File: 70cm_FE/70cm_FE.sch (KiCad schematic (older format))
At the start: 67 parts, among them J1 Conn_01x02, J2 U.FL, J3 U.FL, J4 Conn_01x02, J5 U.FL, Q1 BFU520W, U1 HT7533-1, U2 M68710L, U3 74HC14

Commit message: Add some component values, add SAW footprint, change LNA transistor
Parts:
- added C18: 2p2, Capacitor_SMD:C_0603_1608Metric, symbol Device:C
- added FL1, FL2: AFS434S3, 70cm_FE:AFS434S3, symbol 70cm_FE:AFS434S3
- added R1, R2: 100k, Resistor_SMD:R_0603_1608Metric, symbol Device:R
- C11: value C -> 10p
- C13, C16: value C -> 5p6
- L2: value L -> 15n; footprint Inductor_SMD:L_0603_1608Metric -> Inductor_SMD:L_0402_1005Metric; LCSC (none) -> C27143
- L4: value L -> 15n
- L5: value L -> 68n
- Q1: value BFU520W -> 2SC3356; footprint Package_TO_SOT_SMD:SOT-323_SC-70 -> Package_TO_SOT_SMD:SOT-23; LCSC C111541 -> C9659
- R10: renamed from R8; value 1k -> 2k2
- R24: renamed from R22; value R -> 100k
- R8: renamed from R7; value 2k2 -> 4k7
- U2: footprint 70cm_pa:M68710L -> 70cm_FE:M68710L
- renumbered C18 to C19, C19 to C20, C20 to C21, C21 to C22, J2 to J1, J3 to J2, J1 to J3, R9 to R11, R10 to R12, R11 to R13, R12 to R14, R13 to R15, R14 to R16, R15 to R17, R16 to R18, R17 to R19, R18 to R20, R19 to R21, R20 to R22, R21 to R23, R1 to R3, R2 to R4, R3 to R5, R4 to R6, R5 to R7, R6 to R9
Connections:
- wire segments 92 -> 100
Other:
- note added: "Here could be some filtering,\nalso for harmonics of the TX drive"
- note added: "TODO: driver stage"
- note added: "TODO:\njumpers to bypass SAW filters"
- note added: "TODO:\njumpers to bypass the LNA"
- note removed: "Here could be some filtering,\nat least for harmonics of the TX drive"
- note removed: "Should there be a place\nfor SAW filter here?"
- moved on the sheet: C11, C13, C16, C19, C20, C21, C22, C3, C4, C8, D2, D3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

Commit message: Add driver stage and jumpers, clean up schematic
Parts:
- removed R12, R13: 0, Resistor_SMD:R_0603_1608Metric, symbol Device:R
- added C10: 10p, Capacitor_SMD:C_0402_1005Metric, symbol Device:C
- added C11, C15, C17, C4, C5: 1n, Capacitor_SMD:C_0402_1005Metric, symbol Device:C
- added C13: 10p, Capacitor_SMD:C_0603_1608Metric, symbol Device:C
- added C14, C18: ?, Capacitor_SMD:C_0402_1005Metric, symbol Device:C
- added C32, C33, C34: DNP, Capacitor_SMD:C_0402_1005Metric, symbol Device:C
- added C6: 100p, Capacitor_SMD:C_0603_1608Metric, symbol Device:C
- added D5, D6, D7: BAV99, Package_TO_SOT_SMD:SOT-23, symbol Diode:BAV99
- added JP1, JP2, JP3, JP4, JP5, JP6: ~, 70cm_FE:Jumper-3_0402, symbol 70cm_FE:Jumper_3_Bridged12
- added L1, L6: 68n, Inductor_SMD:L_0603_1608Metric, symbol Device:L
- added L2, L5: 15n?, Inductor_SMD:L_0402_1005Metric, symbol Device:L
- added Q1, Q3: 2SC3356, Package_TO_SOT_SMD:SOT-23, symbol Device:Q_NPN_BEC
- added R1, R3: 100k, Resistor_SMD:R_0402_1005Metric, symbol Device:R
- added R10, R9: 1k, Resistor_SMD:R_0603_1608Metric, symbol Device:R
- added R14, R42: 100, Resistor_SMD:R_0603_1608Metric, symbol Device:R
- added R17, R6: 1, Resistor_SMD:R_0603_1608Metric, symbol Device:R
- added R18: 10, Resistor_SMD:R_0603_1608Metric, symbol Device:R
- added R22, R23, R25, R26, R27: 0, Resistor_SMD:R_0402_1005Metric, symbol Device:R
- added R30, R31, R32, R33, R34, R35: DNP, Resistor_SMD:R_0402_1005Metric, symbol Device:R
- added R7: 4k7, Resistor_SMD:R_0603_1608Metric, symbol Device:R
- C12: renamed from C9; footprint Capacitor_SMD:C_0603_1608Metric -> Capacitor_SMD:C_0402_1005Metric; LCSC (none) -> C1525
- C21: renamed from C10; footprint Capacitor_SMD:C_0603_1608Metric -> Capacitor_SMD:C_0402_1005Metric; LCSC (none) -> C1525
- C7: renamed from C4; value 100n -> 1n; footprint Capacitor_SMD:C_0603_1608Metric -> Capacitor_SMD:C_0402_1005Metric; LCSC (none) -> C1523
- J1: renamed from J3; value Conn_01x02 -> ~
- J5: renamed from J4; value Conn_01x02 -> ~; footprint Connector_PinHeader_2.54mm:PinHeader_1x02_P2.54mm_Vertical -> Connector_PinHeader_2.54mm:PinHeader_1x04_P2.54mm_Vertical; symbol Connector_Generic:Conn_01x02 -> Connector_Generic:Conn_01x04
- L10: renamed from L6; footprint Inductor_SMD:L_0603_1608Metric -> 70cm_FE:NetTie-2_SMD_Pad0.2mm
- L7: renamed from L4; footprint Inductor_SMD:L_0603_1608Metric -> 70cm_FE:NetTie-2_SMD_Pad0.2mm
- L9: renamed from L5; LCSC (none) -> C13415
- R2: renamed from R1; footprint Resistor_SMD:R_0603_1608Metric -> Resistor_SMD:R_0402_1005Metric
- R20: renamed from R24; footprint Resistor_SMD:R_0603_1608Metric -> Resistor_SMD:R_0402_1005Metric
- R21: renamed from R11; footprint Resistor_SMD:R_0603_1608Metric -> Resistor_SMD:R_0402_1005Metric
- R24: renamed from R17; footprint Resistor_SMD:R_0603_1608Metric -> Resistor_SMD:R_0402_1005Metric
- R28: renamed from R19; value 1k -> 100
- R29: renamed from R18; value 0 -> 100k
- R4: renamed from R2; footprint Resistor_SMD:R_0603_1608Metric -> Resistor_SMD:R_0402_1005Metric
- renumbered C8 to C16, C7 to C19, C11 to C20, C13 to C22, C16 to C23, C12 to C24, C19 to C25, C14 to C26, C15 to C27, C20 to C28, C18 to C29, C5 to C3, C21 to C30, C22 to C31, C17 to C35, C3 to C8, C6 to C9, FL2 to FL1, FL1 to FL2, J1 to J2, J2 to J3, J5 to J4, L7 to L11, L1 to L3, L2 to L4, L3 to L8, Q1 to Q2, R7 to R11, R4 to R12, R5 to R13, R8 to R15, R10 to R16, R9 to R19, R14 to R36, R20 to R37, R21 to R38, R22 to R39, R23 to R40, R16 to R41, R15 to R43, R3 to R5, R6 to R8, U3 to U2, U2 to U3
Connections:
- net labels added: DRV_EN, DRV_IN, DRV_OUT, DRV_bias, DRV_bypass, LNA_OUT, PA_EN, PIN_bias, RXSAW_IN, RXSAW_OUT, RXSAW_bypass, TXSAW_bypass, TXSAW_in, TXSAW_out, TX_ON, TX_ON_IN, TX_detect, ~TX_ON~
- net labels removed: PIN_EN, TX_EN, TX_EN_IN, ~TX_EN~
- wire segments 100 -> 176
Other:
- note added: "Control logic.\nDiodes can be used for sequencing delays."
- note added: "For better power handling, some coils are replaced\nwith long, thin microstrip lines.\nWorst-case power loss in 15 nH 0402 coil with Q=20\nfrom JLC basic series could have been around 0.5 W.\n"
- note added: "TODO: LNA bypass jumpers.\nShould the bypass branch include\nprotection diodes or not?"
- note removed: "TODO: driver stage"
- note removed: "TODO:\njumpers to bypass SAW filters"
- note removed: "TODO:\njumpers to bypass the LNA"
- moved on the sheet: C1, C12, C16, C19, C2, C20, C21, C22, C23, C24, C25, C26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

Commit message: Add RF detector, more layout
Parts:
- added C1: 1p, Capacitor_SMD:C_0402_1005Metric, symbol Device:C
- added C33: 10p, Capacitor_SMD:C_0402_1005Metric, symbol Device:C
- added D5: BAT54C, Package_TO_SOT_SMD:SOT-23, symbol Diode:BAT54C
- added R11: DNP, Resistor_SMD:R_0402_1005Metric, symbol Device:R
- added R21, R23: 100k, Resistor_SMD:R_0402_1005Metric, symbol Device:R
- added R22: 220k, Resistor_SMD:R_0402_1005Metric, symbol Device:R
- added R24, R26, R27: 1k, Resistor_SMD:R_0402_1005Metric, symbol Device:R
- added U4: LM393, Package_SO:SOIC-8_3.9x4.9mm_P1.27mm, symbol Comparator:LM393
- R10, R7, R8, R9: footprint Resistor_SMD:R_0603_1608Metric -> Resistor_SMD:R_0402_1005Metric
- R12: renamed from R13; footprint Resistor_SMD:R_0603_1608Metric -> Resistor_SMD:R_0402_1005Metric
- R14: renamed from R12; footprint Resistor_SMD:R_0603_1608Metric -> Resistor_SMD:R_0402_1005Metric
- R15: renamed from R14; footprint Resistor_SMD:R_0603_1608Metric -> Resistor_SMD:R_0402_1005Metric
- R16: renamed from R15; footprint Resistor_SMD:R_0603_1608Metric -> Resistor_SMD:R_0402_1005Metric
- R17: renamed from R16; footprint Resistor_SMD:R_0603_1608Metric -> Resistor_SMD:R_0402_1005Metric
- R19: renamed from R18; footprint Resistor_SMD:R_0603_1608Metric -> Resistor_SMD:R_0402_1005Metric
- R32: renamed from R29; footprint Resistor_SMD:R_0603_1608Metric -> Resistor_SMD:R_0402_1005Metric
- R36: renamed from R28; footprint Resistor_SMD:R_0603_1608Metric -> Resistor_SMD:R_0402_1005Metric
- R44: renamed from R37; footprint Resistor_SMD:R_0603_1608Metric -> Resistor_SMD:R_0402_1005Metric
- R45: renamed from R38; footprint Resistor_SMD:R_0603_1608Metric -> Resistor_SMD:R_0402_1005Metric
- R46: renamed from R39; footprint Resistor_SMD:R_0603_1608Metric -> Resistor_SMD:R_0402_1005Metric
- R47: renamed from R40; footprint Resistor_SMD:R_0603_1608Metric -> Resistor_SMD:R_0402_1005Metric
- R48: renamed from R41; footprint Resistor_SMD:R_0603_1608Metric -> Resistor_SMD:R_0402_1005Metric
- R49: renamed from R42; footprint Resistor_SMD:R_0603_1608Metric -> Resistor_SMD:R_0402_1005Metric
- renumbered C9 to C11, C11 to C12, C12 to C14, C14 to C15, C15 to C16, C16 to C17, C17 to C18, C18 to C19, C1 to C2, C19 to C20, C20 to C21, C21 to C22, C22 to C23, C23 to C24, C24 to C25, C25 to C26, C26 to C27, C27 to C28, C28 to C29, C2 to C3, C29 to C30, C30 to C31, C31 to C32, C32 to C34, C33 to C35, C34 to C36, C35 to C37, C3 to C4, C4 to C5, C5 to C6, C6 to C7, C7 to C8, C8 to C9, D5 to D6, D6 to D7, D7 to D8, R11 to R13, R17 to R18, R19 to R20, R20 to R25, R21 to R28, R22 to R29, R23 to R30, R24 to R31, R25 to R33, R26 to R34, R27 to R35, R30 to R37, R31 to R38, R32 to R39, R33 to R40, R34 to R41, R35 to R42, R36 to R43, R43 to R50
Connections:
- net labels added: DET_IN+, DET_IN-, DET_REF, DET_RF, DET_timing, DRV_B, DRV_C, DRV_E, LNA_B, LNA_C, LNA_E, LNA_VCC, PIN_COMRF, PIN_RXRF, PIN_TXRF, ~LNA_EN_IN~, ~LNA_EN_SEQ~, ~PA_EN_IN~, ~PA_EN_SEQ~, ~PIN_EN_IN~, ~PIN_EN_SEQ~
- wire segments 176 -> 201
- no-connect marks 0 -> 1
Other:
- note added: "TODO:\nshould the spare comparator be used\nfor overtemperature protection?"
- note removed: "TODO: RF detection"
- moved on the sheet: C11, C14, C34, C35, C36, C37, D6, D7, D8, R12, R13, R14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

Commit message: Fix control signal polarities, draft more layout
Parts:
- removed J5: ~, Connector_PinHeader_2.54mm:PinHeader_1x04_P2.54mm_Vertical, symbol Connector_Generic:Conn_01x04
- added C20: 100n, Capacitor_SMD:C_0402_1005Metric, symbol Device:C
- added R32, R44: 100, Resistor_SMD:R_0402_1005Metric, symbol Device:R
- J1: footprint Connector_PinHeader_2.54mm:PinHeader_1x02_P2.54mm_Vertical -> Connector_PinHeader_2.54mm:PinHeader_1x06_P2.54mm_Horizontal; symbol Connector_Generic:Conn_01x02 -> Connector_Generic:Conn_01x06
- R28: renamed from R32; value 100k -> 220k
- R34: renamed from R33; value 0 -> 220k
- R35: renamed from R34; value 0 -> 100k
- R39: renamed from R38; value DNP -> 0; DNP DNP -> (none)
- renumbered C12 to C11, C11 to C12, C20 to C21, C21 to C22, C22 to C23, C23 to C24, C24 to C25, C25 to C26, C26 to C27, C27 to C28, C28 to C29, C29 to C30, C30 to C31, C31 to C32, C32 to C33, C33 to C34, C34 to C35, C35 to C36, C36 to C37, C37 to C38, C5 to C4, C4 to C5, R8 to R10, R12 to R11, R11 to R12, R14 to R13, R13 to R14, R28 to R29, R29 to R30, R30 to R31, R31 to R33, R35 to R36, R36 to R37, R37 to R38, R39 to R40, R40 to R41, R41 to R42, R42 to R43, R43 to R45, R44 to R46, R45 to R47, R46 to R48, R47 to R49, R48 to R50, R49 to R51, R50 to R52, R9 to R8, R10 to R9, U4 to U3, U3 to U4
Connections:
- net labels added: DET_COMP+, DET_COMP-, DET_COMPout, DET_OUT, DET_OUT_
- net labels removed: DET_IN+, DET_IN-, TX_detect
- wire segments 201 -> 202
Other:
- moved on the sheet: C12, C14, C2, C3, C34, C5, D1, R10, R12, R14, R28, R5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

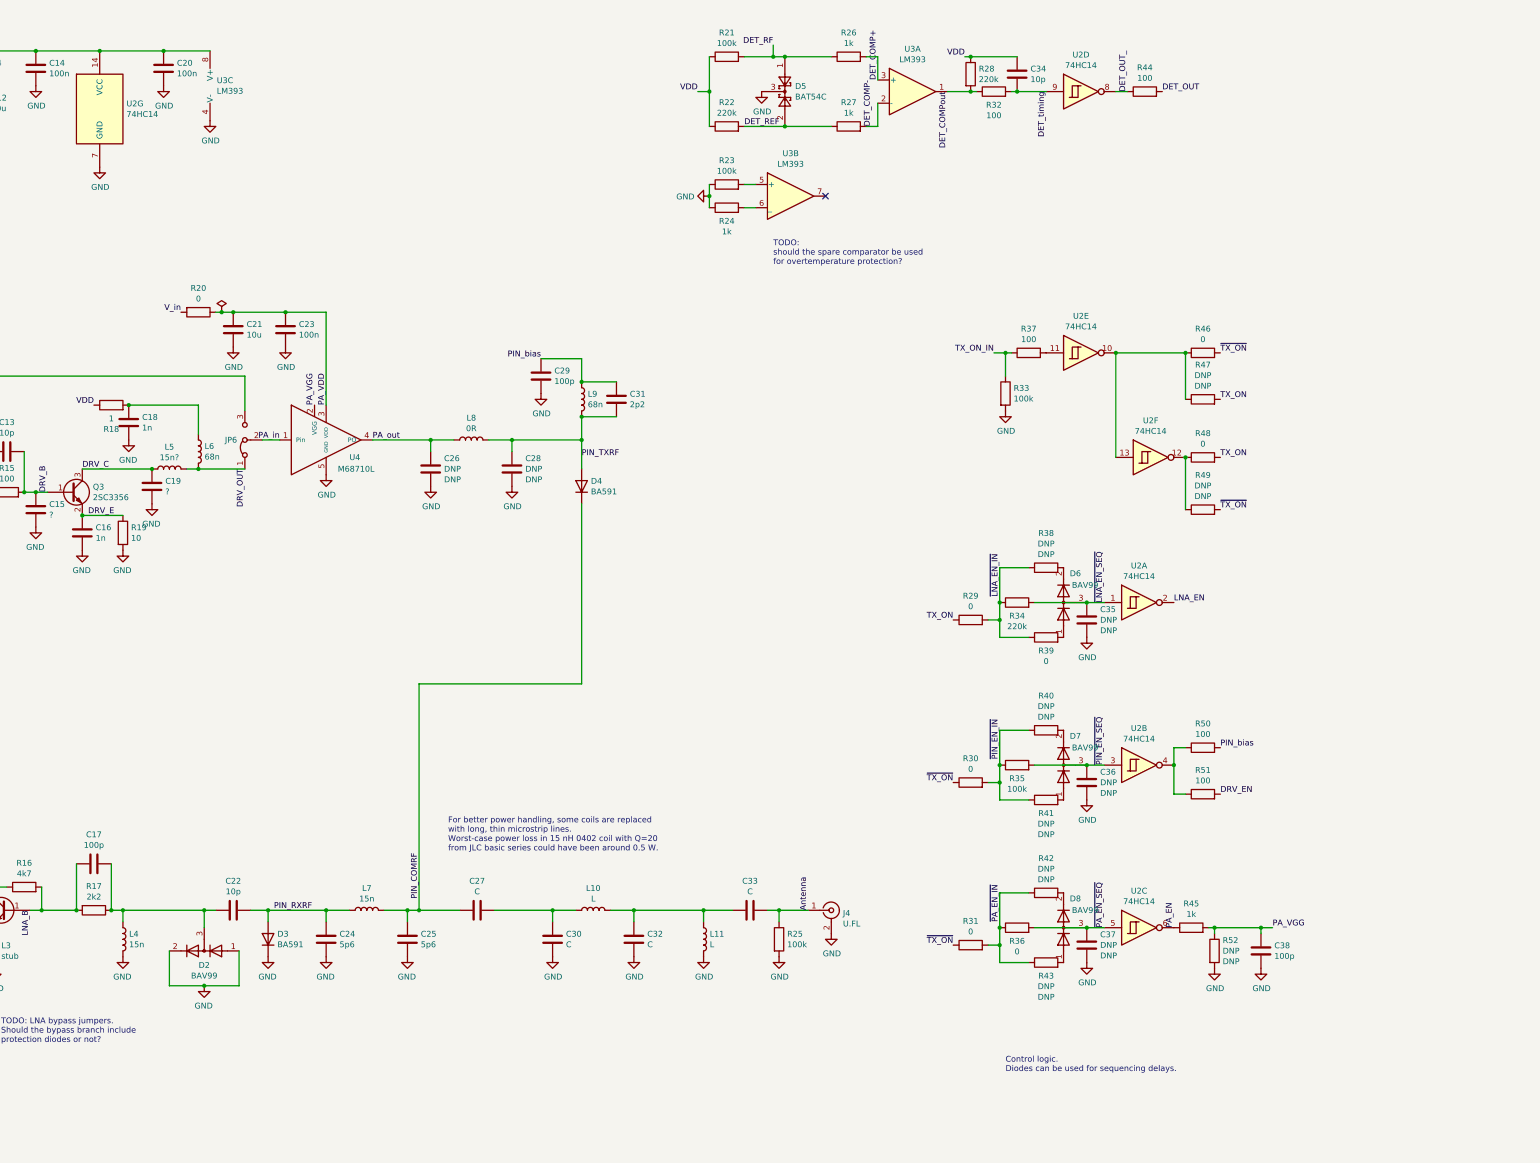
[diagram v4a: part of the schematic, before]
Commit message: Add overtemperature protection
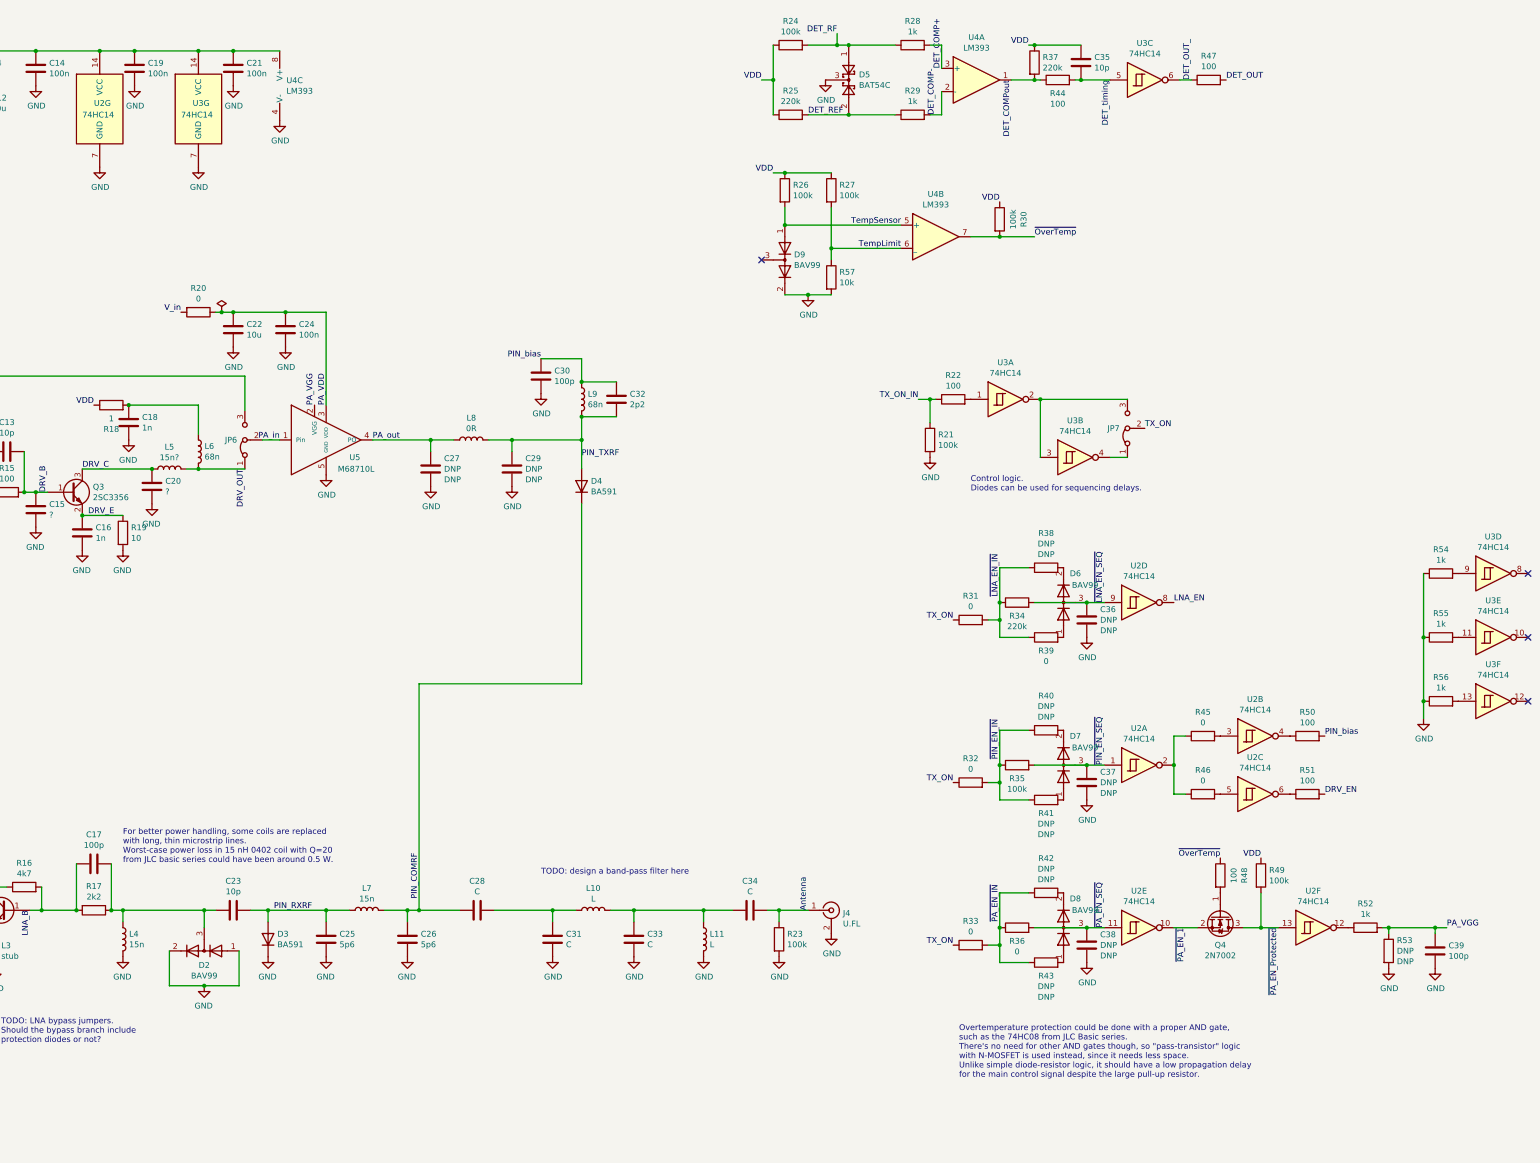
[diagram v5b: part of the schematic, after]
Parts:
- removed R24: 1k, Resistor_SMD:R_0402_1005Metric, symbol Device:R
- removed R47: DNP, Resistor_SMD:R_0402_1005Metric, symbol Device:R
- added C19: 100n, Capacitor_SMD:C_0402_1005Metric, symbol Device:C
- added D9: BAV99, Package_TO_SOT_SMD:SOT-23, symbol Diode:BAV99
- added JP7: ~, 70cm_FE:Jumper-3_0402, symbol 70cm_FE:Jumper_3_Bridged12
- added Q4: 2N7002, Package_TO_SOT_SMD:SOT-23, symbol Transistor_FET:2N7002
- added R27, R30: 100k, Resistor_SMD:R_0402_1005Metric, symbol Device:R
- added R48: 100, Resistor_SMD:R_0402_1005Metric, symbol Device:R
- added R54, R55, R56: 1k, Resistor_SMD:R_0402_1005Metric, symbol Device:R
- added R57: 10k, Resistor_SMD:R_0402_1005Metric, symbol Device:R
- added U3: 74HC14, Package_SO:SOIC-14_3.9x8.7mm_P1.27mm, symbol 74xx:74HC14
- R49: value DNP -> 100k; DNP DNP -> (none)
- renumbered C19 to C20, C20 to C21, C21 to C22, C22 to C23, C23 to C24, C24 to C25, C25 to C26, C26 to C27, C27 to C28, C28 to C29, C29 to C30, C30 to C31, C31 to C32, C32 to C33, C33 to C34, C34 to C35, C35 to C36, C36 to C37, C37 to C38, C38 to C39, R33 to R21, R37 to R22, R25 to R23, R21 to R24, R22 to R25, R23 to R26, R26 to R28, R27 to R29, R29 to R31, R30 to R32, R31 to R33, R28 to R37, R32 to R44, R48 to R45, R44 to R47, R45 to R52, R52 to R53, U3 to U4, U4 to U5
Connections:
- net DET_OUT_: now also U3.6; no longer U2.8
- net DET_timing: now also U3.5; no longer U2.9
- net GND: now also C19.2, D9.2 (A), R54.1, R55.1, R56.1, R57.2, U3.7 (GND); no longer R26.1
- net LNA_EN: now also U2.8; no longer U2.2
- net TX_ON: now also R32.1, R33.1, JP7.2 (C); no longer R45.2
- net VDD: now also R26.1, R49.1, C19.1, R27.1, R30.1, U3.14 (VCC)
- net ~LNA_EN_SEQ~: now also U2.9; no longer U2.1
- net ~PA_EN_SEQ~: now also U2.11; no longer U2.5
- net ~PIN_EN_SEQ~: now also U2.1; no longer U2.3
- net at R50.1, U2.4: no longer R51.1
- net TempSensor: now reaches R26.2, U4.5 (+)
- net TempSensor: now also D9.1 (K)
- net TempLimit: now reaches U4.6 (_)
- net TempLimit: now also R27.2, R57.1
- net ~OverTemp~: now reaches U4.7
- net ~OverTemp~: now also R30.2, R48.1
- net at R22.2: now also U3.1; no longer U2.11
- net PA_EN: no longer names the net of R52.1
- net PA_EN: now also U2.12; no longer U2.6
- removed net ~TX_ON~: R32.1, R33.1, R46.2, R49.2
- new net: R45.1, R46.1, U2.2
- new net: R45.2, U2.3
- new net: JP7.3 (B), U3.2, U3.3
- new net: JP7.1 (A), U3.4
- new net: R54.2, U3.9
- new net: R55.2, U3.11
- new net: R56.2, U3.13
- new net: R46.2, U2.5
- new net: R51.1, U2.6
- new net: Q4.1 (G), R48.2
- new net ~PA_EN_1~: Q4.2 (S), U2.10
- new net ~PA_EN_Protected~: Q4.3 (D), R49.2, U2.13
- no-connect marks 1 -> 4
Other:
- note added: "Overtemperature protection could be done with a proper AND gate,\nsuch as the 74HC08 from JLC Basic series.\nThere's no need for other AND gates though, so "pass-transistor" logic\nwith N-MOSFET is used instead, since it needs less space.\nUnlike simple diode-resistor logic, it should have a low propagation delay\nfor the main control signal despite the large pull-up resistor."
- note added: "TODO: design a band-pass filter here"
- note removed: "TODO:\nshould the spare comparator be used\nfor overtemperature protection?"
- moved on the sheet: C21, C35, C39, D5, R21, R22, R24, R25, R26, R28, R29, R37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
